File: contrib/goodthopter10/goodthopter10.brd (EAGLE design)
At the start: 54.3 x 21.6 mm, 24 parts, among them IC1 F22X4---DA38, IC2 FT232RL-BASICSSOP, Q1 20MHz

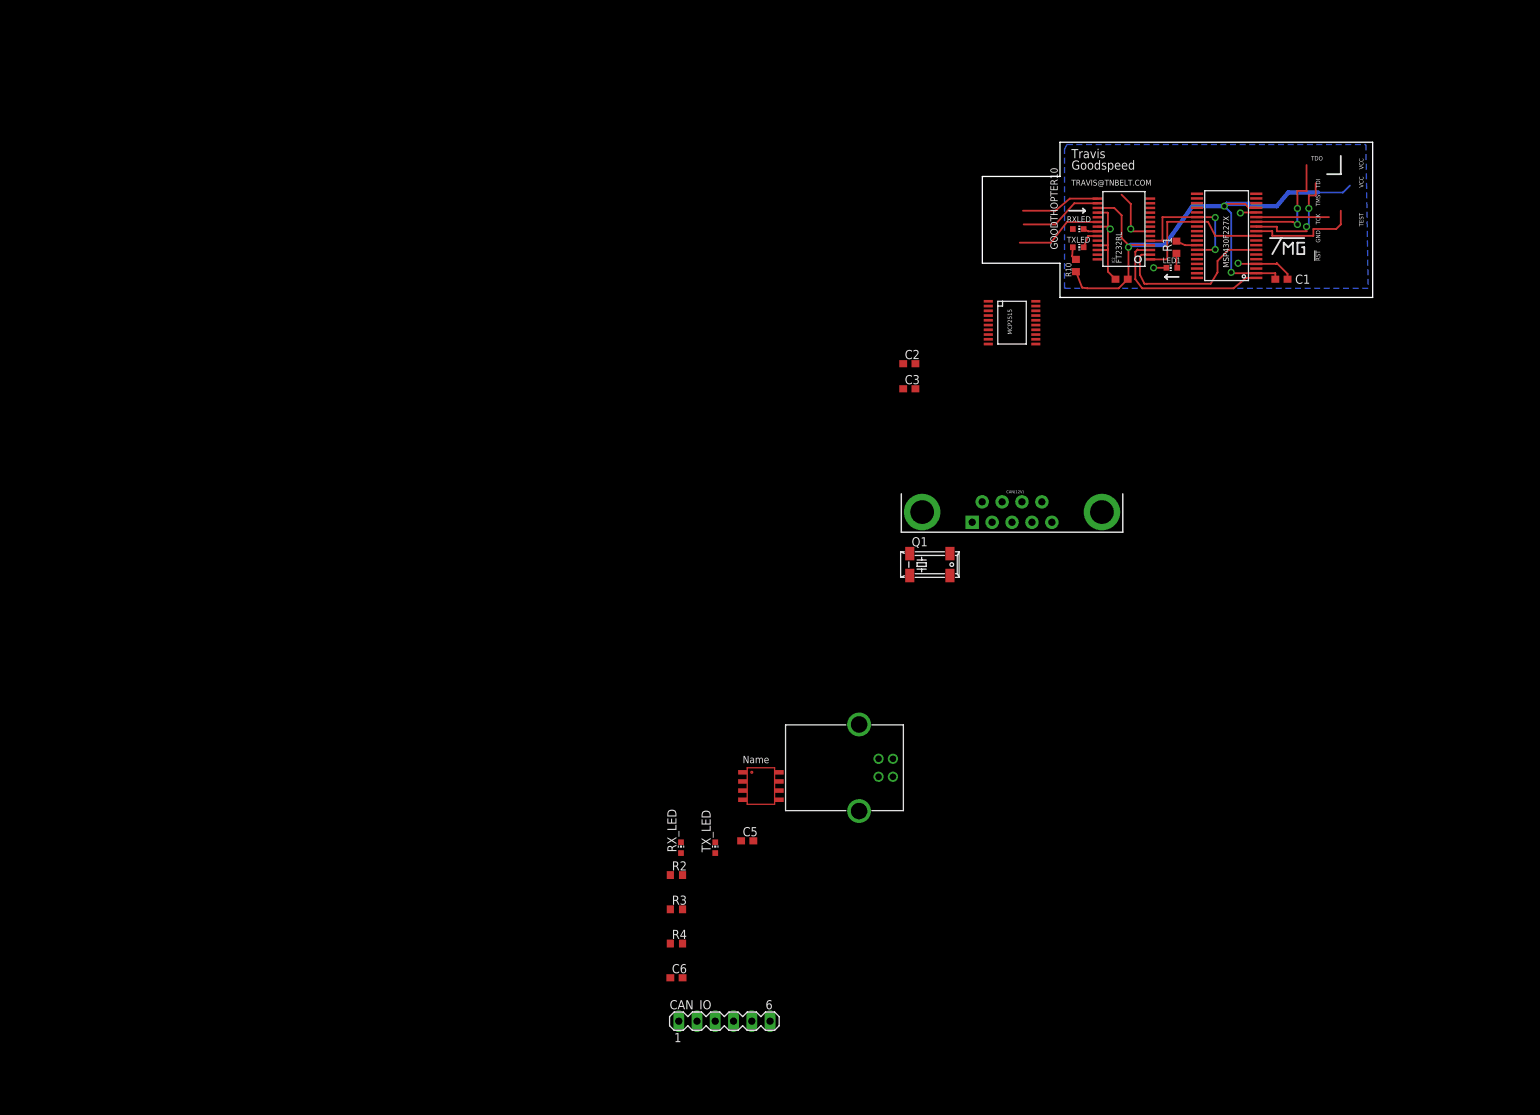
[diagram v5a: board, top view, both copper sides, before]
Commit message: Added BOM to GoodThopter10/, modified SCH and BRD.
git-svn-id: https://svn.code.sf.net/p/goodfet/code@1212 12e2690d-a6be-4b82-a7b7-67c4a43b65c8
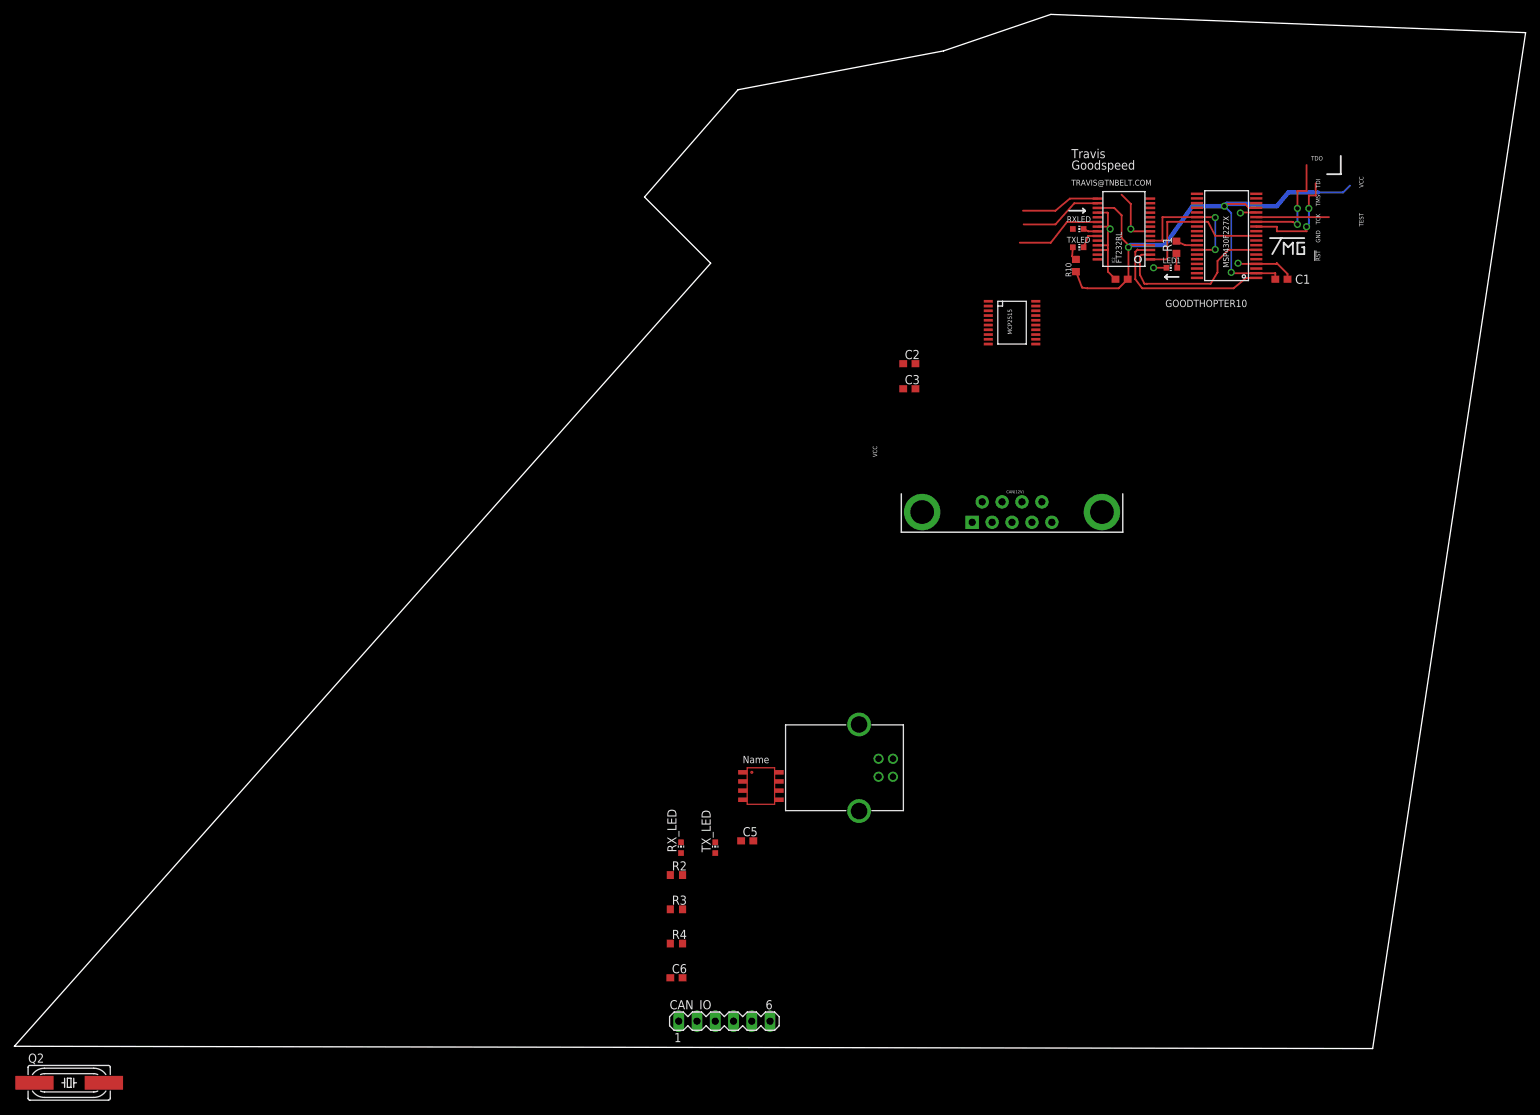
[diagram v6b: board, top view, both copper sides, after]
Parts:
- removed Q1: 20MHz, crystal:MM20SS
- added Q2: 20MHz, crystal:HC49UP
- R10: value 300 -> 330
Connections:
- removed net !CS: IC1.11
- net OSC1: now also Q2.1; no longer Q1.1
- net OSC2: now also Q2.2; no longer Q1.4
- net VCC: now also C5.2, U$2.VDD
- net VCC5V: no longer C5.2, U$2.VDD
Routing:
- net !CS: track 15.5 -> 0.00 mm
- removed copper zone on layer 16, net GND
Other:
- board size 54.3 x 21.6 mm -> 210.2 x 143.8 mm
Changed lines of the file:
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@@
 <layer number="43" name="vRestrict" color="2" fill="10" visible="yes" active="yes"/>
 <layer number="44" name="Drills" color="7" fill="1" visible="no" active="yes"/>
-<layer number="45" name="Holes" color="7" fill="1" visible="no" active="yes"/>
+<layer number="45" name="Holes" color="7" fill="1" visible="yes" active="yes"/>
 <layer number="46" name="Milling" color="3" fill="1" visible="no" active="yes"/>
 <layer number="47" name="Measures" color="7" fill="1" visible="no" active="yes"/>
@@
 <board>
 <plain>
-<wire x1="10.795" y1="0.3175" x2="54.28" y2="0.3175" width="0" layer="20"/>
-<wire x1="54.28" y1="0.3175" x2="54.28" y2="21.9075" width="0" layer="20"/>
-<wire x1="54.28" y1="21.9075" x2="10.795" y2="21.9075" width="0" layer="20"/>
-<wire x1="10.795" y1="21.9075" x2="10.795" y2="17.145" width="0" layer="20"/>
-<wire x1="10.795" y1="17.145" x2="0" y2="17.145" width="0" layer="20"/>
-<wire x1="0" y1="17.145" x2="0" y2="5.08" width="0" layer="20"/>
-<wire x1="0" y1="5.08" x2="10.795" y2="5.08" width="0" layer="20"/>
-<wire x1="10.795" y1="5.08" x2="10.795" y2="0.3175" width="0" layer="20"/>
+<wire x1="-134.62" y1="-103.8225" x2="54.28" y2="-104.14" width="0" layer="20"/>
+<wire x1="54.28" y1="-104.14" x2="75.5525" y2="37.1475" width="0" layer="20"/>
+<wire x1="75.5525" y1="37.1475" x2="9.525" y2="39.6875" width="0" layer="20"/>
+<wire x1="9.525" y1="39.6875" x2="-5.3975" y2="34.6075" width="0" layer="20"/>
+<wire x1="-5.3975" y1="34.6075" x2="-33.9725" y2="29.21" width="0" layer="20"/>
+<wire x1="-33.9725" y1="29.21" x2="-46.99" y2="14.2875" width="0" layer="20"/>
+<wire x1="-46.99" y1="14.2875" x2="-37.7825" y2="5.08" width="0" layer="20"/>
+<wire x1="-37.7825" y1="5.08" x2="-134.62" y2="-103.8225" width="0" layer="20"/>
 <wire x1="47.9425" y1="17.4625" x2="49.8475" y2="17.4625" width="0.254" layer="21"/>
 <wire x1="49.8475" y1="17.4625" x2="49.8475" y2="20.0025" width="0.254" layer="21"/>
@@
 <wire x1="25.7175" y1="3.4925" x2="25.4" y2="3.175" width="0.254" layer="25"/>
 <wire x1="25.4" y1="3.175" x2="25.7175" y2="2.8575" width="0.254" layer="25"/>
-<text x="10.4775" y="6.985" size="1.016" layer="21" font="vector" rot="R90">GOODTHOPTER10</text>
+<text x="36.83" y="0" size="1.016" layer="21" font="vector" rot="R180">GOODTHOPTER10</text>
 <text x="12.3825" y="18.0975" size="1.27" layer="21" font="vector">Goodspeed</text>
 <text x="12.3825" y="19.685" size="1.27" layer="21" font="vector">Travis</text>
@@
 <text x="34.29" y="4.445" size="0.8128" layer="25" font="vector" rot="R90">MSP430F227X</text>
 <text x="19.3675" y="5.08" size="0.8128" layer="25" font="fixed" rot="R90">FT232RL</text>
-<text x="52.3875" y="19.685" size="0.6096" layer="25" font="fixed" rot="R270">VCC</text>
+<text x="-15.24" y="-20.32" size="0.6096" layer="25" font="fixed" rot="R270">VCC</text>
 <text x="52.3875" y="17.145" size="0.6096" layer="25" font="fixed" rot="R270">VCC</text>
 <text x="52.3875" y="12.065" size="0.6096" layer="25" font="fixed" rot="R270">TEST</text>
@@
 <attribute name="VALUE" x="12.7" y="5.3975" size="1.27" layer="27"/>
 </element>
-<element name="R10" library="rcl" package="R0603" value="300" x="13.0175" y="4.7625" smashed="yes" rot="R270">
+<element name="R10" library="rcl" package="R0603" value="330" x="13.0175" y="4.7625" smashed="yes" rot="R270">
 <attribute name="NAME" x="12.3825" y="3.175" size="0.8128" layer="25" font="fixed" rot="R90"/>
 </element>
@@
 <element name="C3" library="rcl" package="C0603" value="15pF" x="-10.16" y="-12.3825"/>
 <element name="CAN(12V)" library="SparkFun-Connectors" package="DB9_MALE" value="" x="4.1275" y="-29.5275"/>
-<element name="Q1" library="crystal" package="MM20SS" value="20MHz" x="-7.3025" y="-36.83">
-<attribute name="OC_NEWARK" value="unknown" x="-7.3025" y="-36.83" size="1.778" layer="27" display="off"/>
-<attribute name="MPN" value="" x="-7.3025" y="-36.83" size="1.778" layer="27" display="off"/>
-<attribute name="MF" value="" x="-7.3025" y="-36.83" size="1.778" layer="27" display="off"/>
-<attribute name="OC_FARNELL" value="unknown" x="-7.3025" y="-36.83" size="1.778" layer="27" display="off"/>
-</element>
 <element name="292304-2" library="USB-TYPE-B" package="85-32004-10X" value="MINI-USB_4P-292304-2" x="-17.145" y="-65.0875">
 <attribute name="OC_NEWARK" value="unknown" x="-17.145" y="-65.0875" size="1.778" layer="27" display="off"/>
@@
 <attribute name="OC_FARNELL" value="unknown" x="-35.8775" y="-100.33" size="1.778" layer="27" display="off"/>
 </element>
+<element name="Q2" library="crystal" package="HC49UP" value="20MHz" x="-127" y="-108.9025">
+<attribute name="OC_NEWARK" value="unknown" x="-127" y="-108.9025" size="1.778" layer="27" display="off"/>
+<attribute name="MPN" value="" x="-127" y="-108.9025" size="1.778" layer="27" display="off"/>
+<attribute name="MF" value="" x="-127" y="-108.9025" size="1.778" layer="27" display="off"/>
+<attribute name="OC_FARNELL" value="unknown" x="-127" y="-108.9025" size="1.778" layer="27" display="off"/>
+</element>
 </elements>
 <signals>
-<signal name="!CS">
-<contactref element="IC1" pad="11"/>
-<wire x1="38.0925" y1="9.54" x2="40.3225" y2="9.54" width="0.254" layer="1"/>
-<wire x1="40.3225" y1="9.54" x2="40.3225" y2="8.89" width="0.254" layer="1"/>
-<wire x1="40.3225" y1="8.89" x2="46.0375" y2="8.89" width="0.254" layer="1"/>
-<wire x1="46.0375" y1="8.89" x2="46.0375" y2="9.8425" width="0.254" layer="1"/>
-<wire x1="46.0375" y1="9.8425" x2="49.2125" y2="9.8425" width="0.254" layer="1"/>
-<wire x1="49.2125" y1="9.8425" x2="49.8475" y2="10.4775" width="0.254" layer="1"/>
-<wire x1="49.8475" y1="10.4775" x2="49.8475" y2="12.3825" width="0.254" layer="1"/>
-</signal>
 <signal name="MOSI">
 <contactref element="IC1" pad="12"/>
@@
 <contactref element="R3" pad="1"/>
 <contactref element="U$1" pad="20"/>
+<contactref element="U$2" pad="VDD"/>
+<contactref element="C5" pad="2"/>
 <wire x1="-43.395" y1="-80.01" x2="-43.395" y2="-84.7725" width="0" layer="19" extent="1-1"/>
-<wire x1="7.4295" y1="-0.2159" x2="-43.395" y2="-80.01" width="0" layer="19" extent="1-1"/>
+<wire x1="-31.8525" y1="-75.2475" x2="-43.395" y2="-80.01" width="0" layer="19" extent="1-1"/>
+<wire x1="-33.3375" y1="-68.2625" x2="-31.8525" y2="-75.2475" width="0" layer="19" extent="1-1"/>
+<wire x1="7.4295" y1="-0.2159" x2="-33.3375" y2="-68.2625" width="0" layer="19" extent="1-1"/>
 <wire x1="13.8675" y1="1.69" x2="7.4295" y2="-0.2159" width="0" layer="19" extent="1-1"/>
 </signal>
@@
 <via x="17.78" y="9.8425" extent="1-16" drill="0.6" shape="square"/>
 <via x="23.8125" y="4.445" extent="1-16" drill="0.6" shape="square"/>
-<polygon width="0.4064" layer="16">
-<vertex x="11.7475" y="21.59"/>
-<vertex x="53.34" y="21.59"/>
-<vertex x="53.6575" y="1.5875"/>
-<vertex x="11.43" y="1.5875"/>
-<vertex x="11.43" y="20.955"/>
-</polygon>
 <contactref element="C2" pad="1"/>
 <contactref element="C3" pad="1"/>
@@
 <wire x1="5.205" y1="7.9375" x2="9.525" y2="7.9375" width="0.254" layer="1"/>
 <contactref element="292304-2" pad="1"/>
-<contactref element="U$2" pad="VDD"/>
-<contactref element="C5" pad="2"/>
-<wire x1="-33.3375" y1="-68.2625" x2="-31.8525" y2="-75.2475" width="0" layer="19" extent="1-1"/>
-<wire x1="-12.435" y1="-66.3375" x2="-33.3375" y2="-68.2625" width="0" layer="19" extent="1-1"/>
 <wire x1="5.205" y1="7.9375" x2="-12.435" y2="-66.3375" width="0" layer="19" extent="1-1"/>
 </signal>
@@
 <contactref element="C3" pad="2"/>
 <contactref element="U$1" pad="9"/>
-<contactref element="Q1" pad="1"/>
-<wire x1="-9.31" y1="-12.3825" x2="-10.0965" y2="-38.354" width="0" layer="19" extent="1-1"/>
+<contactref element="Q2" pad="1"/>
+<wire x1="-9.31" y1="-12.3825" x2="-131.826" y2="-108.9025" width="0" layer="19" extent="1-1"/>
 <wire x1="0.8255" y1="-5.4991" x2="-9.31" y2="-12.3825" width="0" layer="19" extent="1-1"/>
 </signal>
@@
 <contactref element="C2" pad="2"/>
 <contactref element="U$1" pad="8"/>
-<contactref element="Q1" pad="4"/>
-<wire x1="-9.31" y1="-8.89" x2="-10.0965" y2="-35.306" width="0" layer="19" extent="1-1"/>
+<contactref element="Q2" pad="2"/>
+<wire x1="-9.31" y1="-8.89" x2="-122.174" y2="-108.9025" width="0" layer="19" extent="1-1"/>
 <wire x1="0.8255" y1="-4.8387" x2="-9.31" y2="-8.89" width="0" layer="19" extent="1-1"/>
 </signal>

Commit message: Routing goodthopter10.brd, updated.
git-svn-id: https://svn.code.sf.net/p/goodfet/code@1213 12e2690d-a6be-4b82-a7b7-67c4a43b65c8
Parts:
- moved Q2 187.5 mm to (7.62, 21.6), turned to 180 degrees
- moved C6 136.7 mm to (30.5, 21.3)
- moved R4 134.6 mm to (30.5, 23.5)
- moved R3 127.3 mm to (45.7, 6.99)
- moved RX_LED 122.5 mm to (48.9, 6.03), turned to 270 degrees
- moved R2 122.4 mm to (45.7, 4.76)
- moved TX_LED 119.7 mm to (48.9, 6.99), turned to 270 degrees
- moved CAN_IO 116.4 mm to (28.3, -3.17), turned to 180 degrees
- moved C5 113.5 mm to (30.5, 19.1)
- moved U$2 112.1 mm to (38.7, 20.3)
- moved 292304-2 75.9 mm to (-3.17, 9.53)
- moved CAN(12V) 63.4 mm to (54.6, 8.89), turned to 270 degrees
- moved C3 35.8 mm to (9.53, 17.5)
- moved C2 31.1 mm to (6.35, 17.5), turned to 180 degrees
- moved U$1 30.7 mm to (23.8, 20.6)
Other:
- board size 210.2 x 143.8 mm -> 72.7 x 31.8 mm
- board text removed: "!RST"
- board text removed: "GND"
- board text removed: "Goodspeed"
- board text removed: "TCK"
- board text removed: "TDI"
- board text removed: "TDO"
- board text removed: "TEST"
- board text removed: "TMS"
- board text removed: "TRAVIS@TNBELT.COM"
- board text removed: "Travis"
- board text removed: "VCC"

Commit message: Completed GoodThopter10 Routing, Gerbers Added, README.
git-svn-id: https://svn.code.sf.net/p/goodfet/code@1214 12e2690d-a6be-4b82-a7b7-67c4a43b65c8
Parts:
- moved C2 48.9 mm to (54.3, 7.94), turned to 0 degrees
- moved Q2 48.6 mm to (52.7, 3.49), turned to 0 degrees
- moved C3 41.4 mm to (49.8, 7.94), turned to 180 degrees
- moved C5 20.9 mm to (51.1, 15.9), turned to 270 degrees
- moved C6 20.7 mm to (51.1, 19.4), turned to 270 degrees
- moved R3 16.3 mm to (55.6, 20.0)
- moved TX_LED 16.3 mm to (58.7, 20.0)
- moved U$1 16.2 mm to (34.9, 8.89), turned to 90 degrees
- moved R2 16.1 mm to (55.6, 17.5)
- moved RX_LED 15.1 mm to (58.7, 17.5)
- moved R4 14.7 mm to (42.2, 14.6), turned to 270 degrees
- moved IC1 14.7 mm to (35.6, 23.5)
- moved RXLED 12.8 mm to (16.5, 22.2)
- moved R10 12.8 mm to (16.2, 17.1)
- moved TXLED 12.8 mm to (16.5, 19.7)
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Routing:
- net GND: track 38.1 -> 163.2 mm, vias 5 -> 0
- net TXCAN: track 0.00 -> 53.2 mm, vias 0 -> 2
- net RXCAN: track 0.00 -> 49.7 mm, vias 0 -> 2
- net VCC: track 82.7 -> 115.8 mm, vias 3 -> 4
- net OSC2: track 0.00 -> 30.2 mm
- net CANH: track 0.00 -> 26.9 mm, vias 0 -> 1
- net CANL: track 0.00 -> 19.7 mm, vias 0 -> 1
- net N$11: track 0.00 -> 18.8 mm
- net N$5: track 0.00 -> 17.8 mm
- net OSC1: track 0.00 -> 16.8 mm, vias 0 -> 2
- net !INT: track 0.00 -> 16.7 mm, vias 0 -> 2
- net RTS: track 24.0 -> 13.3 mm, vias 0 -> 2
- net VCC5V: track 12.2 -> 21.6 mm
- net DTR: track 24.2 -> 15.0 mm, vias 0 -> 2
- net !TX2RTS: track 0.00 -> 8.43 mm, vias 0 -> 1
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- added copper zone on layer 1, net GND
- added copper zone on layer 16, net GND
